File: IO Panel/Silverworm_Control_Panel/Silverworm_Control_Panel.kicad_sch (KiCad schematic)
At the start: 30 parts, among them J1 Microfit 6-pin, J2 Conn_01x15, J3 Conn_01x15, J4 JST-PH-2PIN, J5 JST-PH-2PIN, J6 JST-PH-2PIN, J7 JST-PH-2PIN, SW1 SW_SPDT

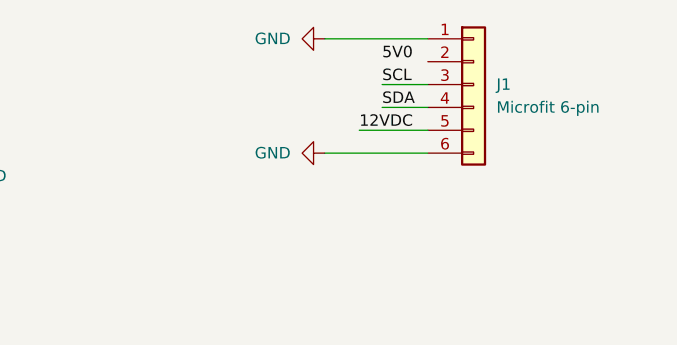
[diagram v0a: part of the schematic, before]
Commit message: Imported PCB outline and layout
Still need to finalise small component placement and routing.
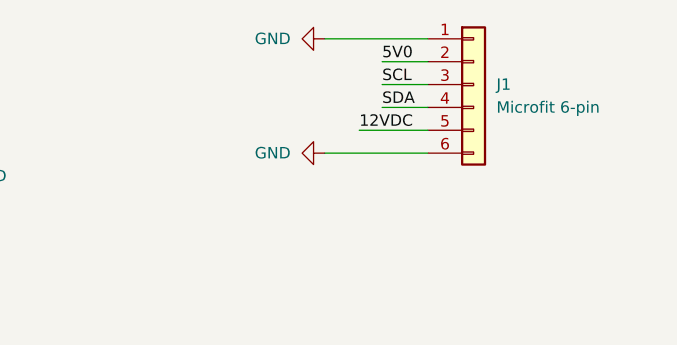
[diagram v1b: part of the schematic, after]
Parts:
- C1, C2, C3, C4: footprint (none) -> Capacitor_Tantalum_SMD:CP_EIA-1608-10_AVX-L
- H1, H2: footprint PEC11R4220KS0024 -> PEC11R-4220K-S0024:PEC11R4220KS0024
- J1: footprint (none) -> Connector_Molex:Molex_Micro-Fit_3.0_43045-0621_2x03-1MP_P3.00mm_Horizontal
- J2, J3: footprint (none) -> Connector_PinSocket_2.54mm:PinSocket_1x15_P2.54mm_Vertical
- J4, J5, J6, J7: footprint (none) -> Connector_JST:JST_PH_B2B-PH-K_1x02_P2.00mm_Vertical
- LED1, LED2: footprint MP008267 -> MP008267_LED:MP008267
- R1, R10, R11, R12, R13, R14, R2, R3, R4, R5, R6, R7, R8, R9: footprint (none) -> Resistor_SMD:R_0603_1608Metric_Pad0.98x0.95mm_HandSolder
- SW1: footprint (none) -> 200MSP1T1B2M2QE:HDRV3W51P470X254_1X3_813X508X2100P
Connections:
- net 5V0: now also J1.2 (Pin_2)
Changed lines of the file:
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@@
 	(wire
 		(pts
+			(xy 251.46 22.86) (xy 256.54 22.86)
+		)
+		(stroke
+			(width 0)
+			(type default)
+		)
+	)
+	(wire
+		(pts
 			(xy 63.5 147.32) (xy 62.23 147.32)
 		)
@@
 			)
 		)
-		(property "Footprint" ""
+		(property "Footprint" "Capacitor_Tantalum_SMD:CP_EIA-1608-10_AVX-L"
 			(at 74.6252 78.74 0)
 			(effects
@@
 			)
 		)
-		(property "Footprint" ""
+		(property "Footprint" "Resistor_SMD:R_0603_1608Metric_Pad0.98x0.95mm_HandSolder"
 			(at 67.31 70.358 90)
 			(effects
@@
 			)
 		)
-		(property "Footprint" ""
+		(property "Footprint" "Resistor_SMD:R_0603_1608Metric_Pad0.98x0.95mm_HandSolder"
 			(at 60.452 76.2 90)
 			(effects
@@
 			)
 		)
-		(property "Footprint" ""
+		(property "Footprint" "Capacitor_Tantalum_SMD:CP_EIA-1608-10_AVX-L"
 			(at 34.5948 78.74 0)
 			(effects
@@
 			)
 		)
-		(property "Footprint" ""
+		(property "Footprint" "Resistor_SMD:R_0603_1608Metric_Pad0.98x0.95mm_HandSolder"
 			(at 121.92 135.382 90)
 			(effects
@@
 			)
 		)
-		(property "Footprint" ""
+		(property "Footprint" "Resistor_SMD:R_0603_1608Metric_Pad0.98x0.95mm_HandSolder"
 			(at 157.48 133.858 90)
 			(effects
@@
 			)
 		)
-		(property "Footprint" ""
+		(property "Footprint" "Resistor_SMD:R_0603_1608Metric_Pad0.98x0.95mm_HandSolder"
 			(at 48.768 154.94 90)
 			(effects
@@
 			)
 		)
-		(property "Footprint" ""
+		(property "Footprint" "Resistor_SMD:R_0603_1608Metric_Pad0.98x0.95mm_HandSolder"
 			(at 121.92 111.252 90)
 			(effects
@@
 			)
 		)
-		(property "Footprint" ""
+		(property "Footprint" "Connector_JST:JST_PH_B2B-PH-K_1x02_P2.00mm_Vertical"
 			(at 135.89 27.94 0)
 			(effects
@@
 			)
 		)
-		(property "Footprint" ""
+		(property "Footprint" "Connector_JST:JST_PH_B2B-PH-K_1x02_P2.00mm_Vertical"
 			(at 135.89 66.04 0)
 			(effects
@@
 			)
 		)
-		(property "Footprint" ""
+		(property "Footprint" "Resistor_SMD:R_0603_1608Metric_Pad0.98x0.95mm_HandSolder"
 			(at 121.92 133.858 90)
 			(effects
@@
 			)
 		)
-		(property "Footprint" "MP008267"
+		(property "Footprint" "MP008267_LED:MP008267"
 			(at 149.86 106.68 0)
 			(effects
@@
 			)
 		)
-		(property "Footprint" ""
+		(property "Footprint" "Connector_PinSocket_2.54mm:PinSocket_1x15_P2.54mm_Vertical"
 			(at 240.03 135.89 0)
 			(effects
@@
 			)
 		)
-		(property "Footprint" ""
+		(property "Footprint" "Resistor_SMD:R_0603_1608Metric_Pad0.98x0.95mm_HandSolder"
 			(at 48.768 76.2 90)
 			(effects
@@
 			)
 		)
-		(property "Footprint" ""
+		(property "Footprint" "Connector_PinSocket_2.54mm:PinSocket_1x15_P2.54mm_Vertical"
 			(at 220.98 135.89 0)
 			(effects
@@
 			)
 		)
-		(property "Footprint" ""
+		(property "Footprint" "Capacitor_Tantalum_SMD:CP_EIA-1608-10_AVX-L"
 			(at 34.5948 157.48 0)
 			(effects
@@
 			)
 		)
-		(property "Footprint" ""
+		(property "Footprint" "Connector_JST:JST_PH_B2B-PH-K_1x02_P2.00mm_Vertical"
 			(at 135.89 53.34 0)
 			(effects
@@
 			)
 		)
-		(property "Footprint" ""
+		(property "Footprint" "Resistor_SMD:R_0603_1608Metric_Pad0.98x0.95mm_HandSolder"
 			(at 121.92 109.728 90)
 			(effects
@@
 			)
 		)
-		(property "Footprint" ""
+		(property "Footprint" "200MSP1T1B2M2QE:HDRV3W51P470X254_1X3_813X508X2100P"
 			(at 196.85 33.02 0)
 			(effects
@@
 			)
 		)
-		(property "Footprint" ""
+		(property "Footprint" "Resistor_SMD:R_0603_1608Metric_Pad0.98x0.95mm_HandSolder"
 			(at 41.91 149.098 90)
 			(effects
@@
 			)
 		)
-		(property "Footprint" "PEC11R4220KS0024"
+		(property "Footprint" "PEC11R-4220K-S0024:PEC11R4220KS0024"
 			(at 63.5 207.95 0)
 			(effects
@@
 			)
 		)
-		(property "Footprint" ""
+		(property "Footprint" "Resistor_SMD:R_0603_1608Metric_Pad0.98x0.95mm_HandSolder"
 			(at 67.31 149.098 90)
 			(effects
@@
 			)
 		)
-		(property "Footprint" ""
+		(property "Footprint" "Resistor_SMD:R_0603_1608Metric_Pad0.98x0.95mm_HandSolder"
 			(at 41.91 70.358 90)
 			(effects
@@
 			)
 		)
-		(property "Footprint" "MP008267"
+		(property "Footprint" "MP008267_LED:MP008267"
 			(at 149.86 130.81 0)
 			(effects
@@
 			)
 		)
-		(property "Footprint" ""
+		(property "Footprint" "Resistor_SMD:R_0603_1608Metric_Pad0.98x0.95mm_HandSolder"
 			(at 157.48 109.728 90)
 			(effects
@@
 			)
 		)
-		(property "Footprint" ""
+		(property "Footprint" "Resistor_SMD:R_0603_1608Metric_Pad0.98x0.95mm_HandSolder"
 			(at 60.452 154.94 90)
 			(effects
@@
 			)
 		)
-		(property "Footprint" ""
+		(property "Footprint" "Capacitor_Tantalum_SMD:CP_EIA-1608-10_AVX-L"
 			(at 74.6252 157.48 0)
 			(effects
@@
 			)
 		)
-		(property "Footprint" "PEC11R4220KS0024"
+		(property "Footprint" "PEC11R-4220K-S0024:PEC11R4220KS0024"
 			(at 63.5 129.21 0)
 			(effects
@@
 			)
 		)
-		(property "Footprint" ""
+		(property "Footprint" "Connector_Molex:Molex_Micro-Fit_3.0_43045-0621_2x03-1MP_P3.00mm_Horizontal"
 			(at 261.62 25.4 0)
 			(effects
@@
 			)
 		)
-		(property "Footprint" ""
+		(property "Footprint" "Connector_JST:JST_PH_B2B-PH-K_1x02_P2.00mm_Vertical"
 			(at 135.89 40.64 0)
 			(effects

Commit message: Layout and IO edits
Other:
- note added: "Buttons and LEDs"
- note added: "Encoders"
- moved on the sheet: C1, C2, C3, C4, H1, H2, J1, J2, J3, J4, J5, J6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

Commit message: Updates
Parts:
- H1, H2: Price (none) -> 1.96; Supplier (none) -> Farnell; Supplier Link (none) -> https://uk.farnell.com/bourns/pec11r-4020f-s0024/incrementa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
- J1: Manufacturer_Part_Number (none) -> 430450621; Price (none) -> 2.28; Supplier (none) -> Farnell; Supplier Link (none) -> https://uk.farnell.com/molex/43045-0621/connector-header-6p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
- J2, J3: Manufacturer_Part_Number (none) -> M20-7821546; Price (none) -> 1.86; Supplier (none) -> Farnell; Supplier Link (none) -> https://uk.farnell.com/harwin/m20-7821546/connector-rcpt-15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
- J4, J5, J6, J7: value JST-PH-2PIN -> JST-XH-2PIN; footprint Connector_JST:JST_PH_B2B-PH-K_1x02_P2.00mm_Vertical -> (none); Manufacturer_Part_Number (none) -> B2B-XH-A(LF)(SN); Price (none) -> 0.83; Supplier (none) -> RS; Supplier Link (none) -> https://uk.rs-online.com/web/p/pcb-headers/8201554
- LED1, LED2: Price (none) -> 1.12; Supplier (none) -> Farnell; Supplier Link (none) -> https://uk.farnell.com/multicomp-pro/mp008267/led-rgb-600mc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
- SW1: Manufacturer_Part_Number (none) -> 200MSP1T1B2M2QE; Price (none) -> 2.23; Supplier (none) -> Mouser; Supplier Link (none) -> https://www.mouser.co.uk/ProductDetail/E-Switch/200MSP1T1B2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
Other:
- note added: "Board Connector"
- moved on the sheet: C1, C2, C3, C4, H1, H2, J1, J2, J3, R1, R2, R3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

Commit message: control panel etc data
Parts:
- added H3: MountingHole, CustomLibrary:MountingHole_17mm_Pad_TopBottom, symbol Mechanical:MountingHole
- J6, J7: now not fitted; now left out of the parts list
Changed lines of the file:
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@@
 		(mirror x)
 		(unit 1)
-		(exclude_from_sim no)
-		(in_bom yes)
-		(on_board yes)
-		(dnp no)
+		(exclude_from_sim yes)
+		(in_bom no)
+		(on_board no)
+		(dnp yes)
 		(fields_autoplaced yes)
 		(property "Reference" "#PWR020"
@@
 		(at 113.03 71.12 0)
 		(unit 1)
-		(exclude_from_sim no)
-		(in_bom yes)
-		(on_board yes)
-		(dnp no)
+		(exclude_from_sim yes)
+		(in_bom no)
+		(on_board no)
+		(dnp yes)
 		(fields_autoplaced yes)
 		(property "Reference" "J7"
@@
 	)
 	(symbol
+		(lib_id "Mechanical:MountingHole")
+		(at 139.7 34.29 0)
+		(unit 1)
+		(exclude_from_sim no)
+		(in_bom no)
+		(on_board yes)
+		(dnp no)
+		(fields_autoplaced yes)
+		(property "Reference" "H3"
+			(at 142.24 33.0199 0)
+			(effects
+				(font
+					(size 1.27 1.27)
+				)
+				(justify left)
+			)
+		)
+		(property "Value" "MountingHole"
+			(at 142.24 35.5599 0)
+			(effects
+				(font
+					(size 1.27 1.27)
+				)
+				(justify left)
+			)
+		)
+		(property "Footprint" "CustomLibrary:MountingHole_17mm_Pad_TopBottom"
+			(at 139.7 34.29 0)
+			(effects
+				(font
+					(size 1.27 1.27)
+				)
+				(hide yes)
+			)
+		)
+		(property "Datasheet" "~"
+			(at 139.7 34.29 0)
+			(effects
+				(font
+					(size 1.27 1.27)
+				)
+				(hide yes)
+			)
+		)
+		(property "Description" "Mounting Hole without connection"
+			(at 139.7 34.29 0)
+			(effects
+				(font
+					(size 1.27 1.27)
+				)
+				(hide yes)
+			)
+		)
+		(instances
+			(project ""
+				(path "/fce682f0-b5dc-4d2c-ad56-13dd102e7c25"
+					(reference "H3")
+					(unit 1)
+				)
+			)
+		)
+	)
+	(symbol
 		(lib_id "Device:C")
 		(at 29.21 168.91 0)
@@
 		(at 113.03 58.42 0)
 		(unit 1)
-		(exclude_from_sim no)
-		(in_bom yes)
-		(on_board yes)
-		(dnp no)
+		(exclude_from_sim yes)
+		(in_bom no)
+		(on_board no)
+		(dnp yes)
 		(fields_autoplaced yes)
 		(property "Reference" "J6"
@@
 		(mirror x)
 		(unit 1)
-		(exclude_from_sim no)
-		(in_bom yes)
-		(on_board yes)
-		(dnp no)
+		(exclude_from_sim yes)
+		(in_bom no)
+		(on_board no)
+		(dnp yes)
 		(fields_autoplaced yes)
 		(property "Reference" "#PWR019"

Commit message: conytrol panel
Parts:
- added TP1: 5V0 Testpoint, TestPoint:TestPoint_THTPad_D2.5mm_Drill1.2mm, symbol Connector:TestPoint
- added TP2: GND Testpoint, TestPoint:TestPoint_Pad_D3.0mm, symbol Connector:TestPoint
- added TP3: 3V3 Testpoint, TestPoint:TestPoint_THTPad_D2.5mm_Drill1.2mm, symbol Connector:TestPoint
- C1, C2, C3, C4: footprint Capacitor_Tantalum_SMD:CP_EIA-1608-10_AVX-L -> Capacitor_SMD:C_0805_2012Metric_Pad1.18x1.45mm_HandSolder
- J4, J5: footprint (none) -> Connector_JST:JST_PH_B2B-PH-K_1x02_P2.00mm_Vertical
- R1, R10, R11, R12, R13, R14, R2, R3, R4, R5, R6, R7, R8, R9: footprint Resistor_SMD:R_0603_1608Metric_Pad0.98x0.95mm_HandSolder -> Resistor_SMD:R_0805_2012Metric_Pad1.20x1.40mm_HandSolder
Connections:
- net 3V3: now also TP3.1
- net 5V0: now also TP1.1
- net GND: now also TP2.1
